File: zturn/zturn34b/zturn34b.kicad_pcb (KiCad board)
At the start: 4 copper layers, 56.5 x 54 mm, 27 parts, among them U1 74AXP4T245, U2 74AXP4T245, U3 74AXP4T245, U4 74AXP4T245, U5 74AXP4T245

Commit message: update net names on zturn pcbs to match active high/low signal type
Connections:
- net /_rMA renamed /r_MA
- net /iBEMA renamed /i_BEMA
- net /iMEM07 renamed /iMEM_07
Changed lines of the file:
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@@
   (net 13 "/pMA07")
   (net 14 "/i_MEMDONE")
-  (net 15 "/_rMA")
+  (net 15 "/r_MA")
   (net 16 "unconnected-(U5-2B1-Pad11)")
   (net 17 "unconnected-(U5-1B1-Pad13)")
@@
   (net 33 "/MEMBUSN")
   (net 34 "/x_MEM")
-  (net 35 "/iBEMA")
-  (net 36 "/iMEM07")
+  (net 35 "/i_BEMA")
+  (net 36 "/iMEM_07")
   (net 37 "/i_EMA")
   (net 38 "/j_STROBE")
@@
       (net 34 "/x_MEM") (pinfunction "Pin_21") (pintype "passive"))
     (pad "22" thru_hole oval (at 2.54 25.4 90) (size 1.7 1.7) (drill 1) (layers "*.Cu" "*.Mask")
-      (net 15 "/_rMA") (pinfunction "Pin_22") (pintype "passive"))
+      (net 15 "/r_MA") (pinfunction "Pin_22") (pintype "passive"))
     (pad "23" thru_hole oval (at 0 27.94 90) (size 1.7 1.7) (drill 1) (layers "*.Cu" "*.Mask")
       (net 19 "GND") (pinfunction "Pin_23") (pintype "passive"))
@@
       (net 19 "GND") (pinfunction "Pin_24") (pintype "passive"))
     (pad "25" thru_hole oval (at 0 30.48 90) (size 1.7 1.7) (drill 1) (layers "*.Cu" "*.Mask")
-      (net 35 "/iBEMA") (pinfunction "Pin_25") (pintype "passive"))
+      (net 35 "/i_BEMA") (pinfunction "Pin_25") (pintype "passive"))
     (pad "26" thru_hole oval (at 2.54 30.48 90) (size 1.7 1.7) (drill 1) (layers "*.Cu" "*.Mask")
-      (net 36 "/iMEM07") (pinfunction "Pin_26") (pintype "passive"))
+      (net 36 "/iMEM_07") (pinfunction "Pin_26") (pintype "passive"))
     (pad "27" thru_hole oval (at 0 33.02 90) (size 1.7 1.7) (drill 1) (layers "*.Cu" "*.Mask")
       (net 19 "GND") (pinfunction "Pin_27") (pintype "passive"))
@@
       (net 10 "/pMA04") (pinfunction "1B1") (pintype "tri_state"))
     (pad "14" smd roundrect (at 2.8625 -0.975 90) (size 1.475 0.4) (layers "F.Cu" "F.Paste" "F.Mask") (roundrect_rratio 0.25)
-      (net 15 "/_rMA") (pinfunction "2OE") (pintype "input"))
+      (net 15 "/r_MA") (pinfunction "2OE") (pintype "input"))
     (pad "15" smd roundrect (at 2.8625 -1.625 90) (size 1.475 0.4) (layers "F.Cu" "F.Paste" "F.Mask") (roundrect_rratio 0.25)
-      (net 15 "/_rMA") (pinfunction "1OE") (pintype "input"))
+      (net 15 "/r_MA") (pinfunction "1OE") (pintype "input"))
     (pad "16" smd roundrect (at 2.8625 -2.275 90) (size 1.475 0.4) (layers "F.Cu" "F.Paste" "F.Mask") (roundrect_rratio 0.25)
       (net 20 "+5V") (pinfunction "VCCB") (pintype "power_in"))
@@
       (net 2 "/pMA00") (pinfunction "1B1") (pintype "tri_state"))
     (pad "14" smd roundrect (at 2.8625 -0.975 90) (size 1.475 0.4) (layers "F.Cu" "F.Paste" "F.Mask") (roundrect_rratio 0.25)
-      (net 15 "/_rMA") (pinfunction "2OE") (pintype "input"))
+      (net 15 "/r_MA") (pinfunction "2OE") (pintype "input"))
     (pad "15" smd roundrect (at 2.8625 -1.625 90) (size 1.475 0.4) (layers "F.Cu" "F.Paste" "F.Mask") (roundrect_rratio 0.25)
-      (net 15 "/_rMA") (pinfunction "1OE") (pintype "input"))
+      (net 15 "/r_MA") (pinfunction "1OE") (pintype "input"))
     (pad "16" smd roundrect (at 2.8625 -2.275 90) (size 1.475 0.4) (layers "F.Cu" "F.Paste" "F.Mask") (roundrect_rratio 0.25)
       (net 20 "+5V") (pinfunction "VCCB") (pintype "power_in"))
@@
       (net 47 "+3V3") (pintype "passive"))
     (pad "2" smd roundrect (at 0.32 0 180) (size 0.46 0.4) (layers "B.Cu" "B.Mask") (roundrect_rratio 0.25)
-      (net 15 "/_rMA") (pintype "passive"))
+      (net 15 "/r_MA") (pintype "passive"))
     (model "${KICAD6_3DMODEL_DIR}/Resistor_SMD.3dshapes/R_0201_0603Metric.wrl"
       (offset (xyz 0 0 0))
@@
       (net 9 "/pMA11") (pinfunction "1B1") (pintype "tri_state"))
     (pad "14" smd roundrect (at 2.8625 0.975 90) (size 1.475 0.4) (layers "B.Cu" "B.Paste" "B.Mask") (roundrect_rratio 0.25)
-      (net 15 "/_rMA") (pinfunction "2OE") (pintype "input"))
+      (net 15 "/r_MA") (pinfunction "2OE") (pintype "input"))
     (pad "15" smd roundrect (at 2.8625 1.625 90) (size 1.475 0.4) (layers "B.Cu" "B.Paste" "B.Mask") (roundrect_rratio 0.25)
-      (net 15 "/_rMA") (pinfunction "1OE") (pintype "input"))
+      (net 15 "/r_MA") (pinfunction "1OE") (pintype "input"))
     (pad "16" smd roundrect (at 2.8625 2.275 90) (size 1.475 0.4) (layers "B.Cu" "B.Paste" "B.Mask") (roundrect_rratio 0.25)
       (net 20 "+5V") (pinfunction "VCCB") (pintype "power_in"))

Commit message: update software and further updates to firmware/pcbs
...for invertering transistors

./z8lsimtest works
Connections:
- net /iMEM_07 renamed /i_MEM_07
- net /i_BEMA renamed /iBEMA
- net /i_EMA renamed /iEMA
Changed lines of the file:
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@@
   (net 33 "/MEMBUSN")
   (net 34 "/x_MEM")
-  (net 35 "/i_BEMA")
-  (net 36 "/iMEM_07")
-  (net 37 "/i_EMA")
+  (net 35 "/iBEMA")
+  (net 36 "/i_MEM_07")
+  (net 37 "/iEMA")
   (net 38 "/j_STROBE")
   (net 39 "/j_EA")
@@
       (net 19 "GND") (pinfunction "Pin_24") (pintype "passive"))
     (pad "25" thru_hole oval (at 0 30.48 90) (size 1.7 1.7) (drill 1) (layers "*.Cu" "*.Mask")
-      (net 35 "/i_BEMA") (pinfunction "Pin_25") (pintype "passive"))
+      (net 35 "/iBEMA") (pinfunction "Pin_25") (pintype "passive"))
     (pad "26" thru_hole oval (at 2.54 30.48 90) (size 1.7 1.7) (drill 1) (layers "*.Cu" "*.Mask")
-      (net 36 "/iMEM_07") (pinfunction "Pin_26") (pintype "passive"))
+      (net 36 "/i_MEM_07") (pinfunction "Pin_26") (pintype "passive"))
     (pad "27" thru_hole oval (at 0 33.02 90) (size 1.7 1.7) (drill 1) (layers "*.Cu" "*.Mask")
       (net 19 "GND") (pinfunction "Pin_27") (pintype "passive"))
@@
       (net 19 "GND") (pinfunction "Pin_28") (pintype "passive"))
     (pad "29" thru_hole oval (at 0 35.56 90) (size 1.7 1.7) (drill 1) (layers "*.Cu" "*.Mask")
-      (net 37 "/i_EMA") (pinfunction "Pin_29") (pintype "passive"))
+      (net 37 "/iEMA") (pinfunction "Pin_29") (pintype "passive"))
     (pad "30" thru_hole oval (at 2.54 35.56 90) (size 1.7 1.7) (drill 1) (layers "*.Cu" "*.Mask")
       (net 1 "/i_EA") (pinfunction "Pin_30") (pintype "passive"))

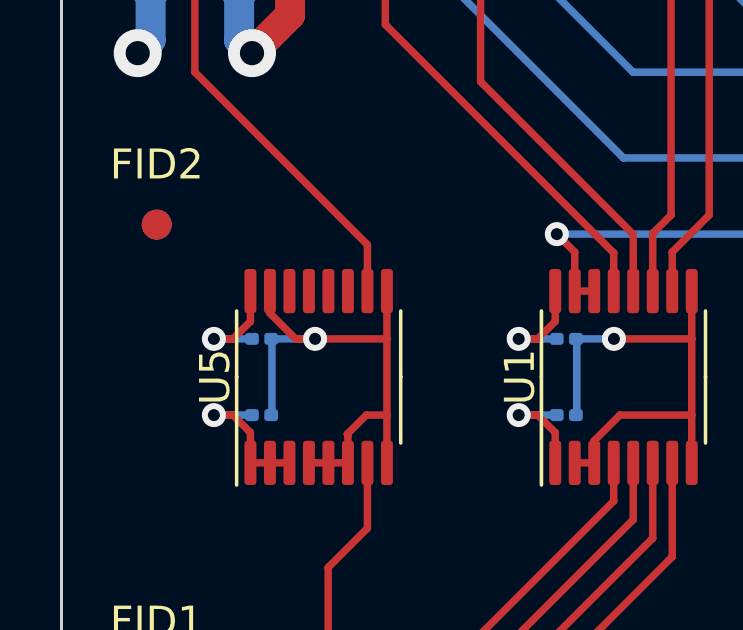
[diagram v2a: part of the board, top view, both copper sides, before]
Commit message: fixed polarity of bus signals for the open-drain transistors
    PDP         Zynq
    MEM         _MEM
    MEM_P       _MEM_P
    _DMAADDR    DMAADDR
    _DMADATA    DMADATA
    _INPUTBUS   INPUTBUS

Also fixed MEMINCR polarity and fixed missing ground connection on circuit board.
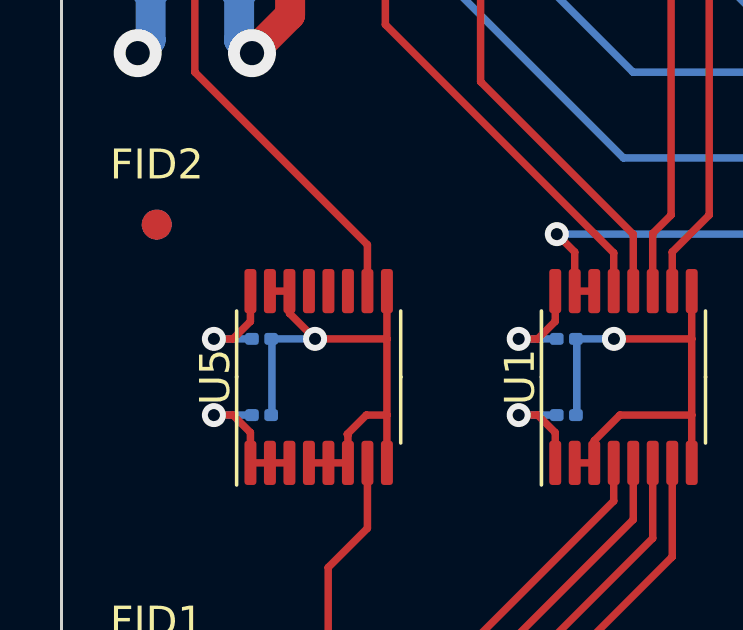
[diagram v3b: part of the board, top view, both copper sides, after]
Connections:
- U5 pad 14: unconnected-(U5-2OE-Pad14) -> GND

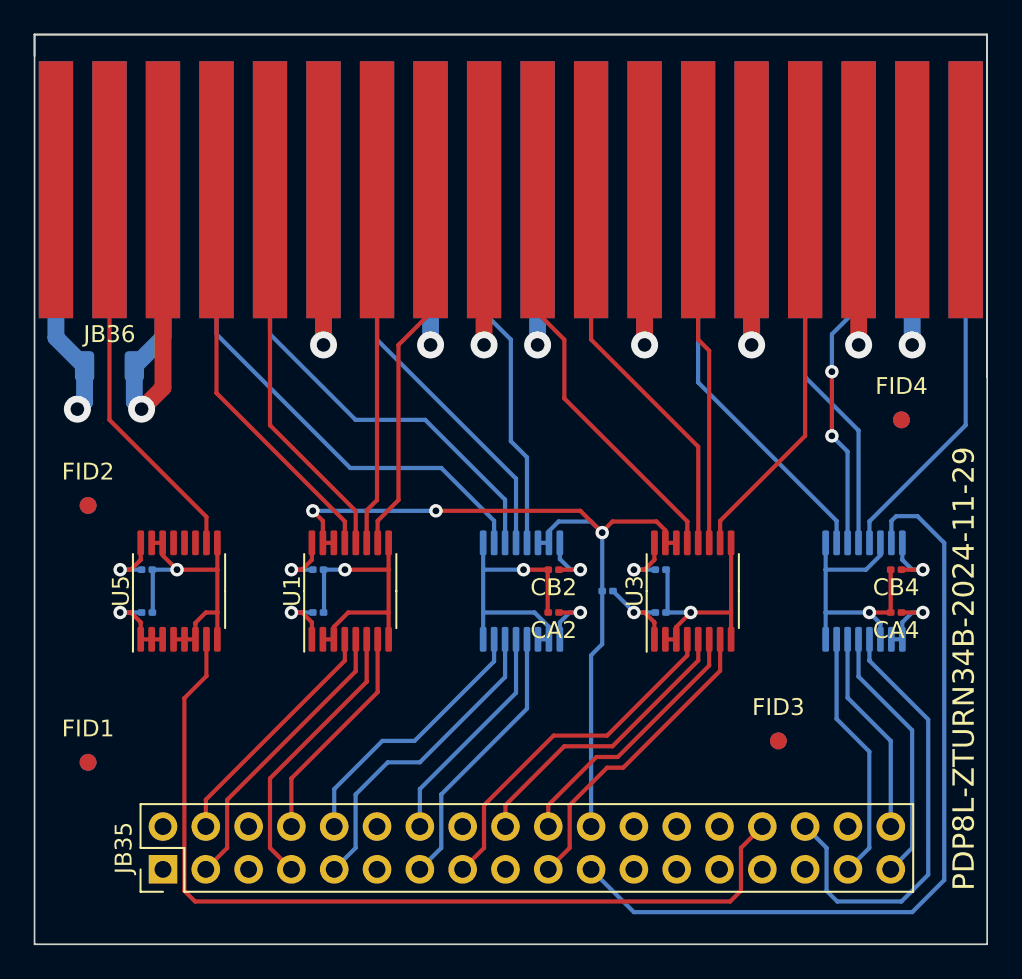
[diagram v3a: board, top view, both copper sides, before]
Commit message: update zturn34b pcb legend and clean up some traces
fixed the i_EA driver output enable dec 26, but legend not updated
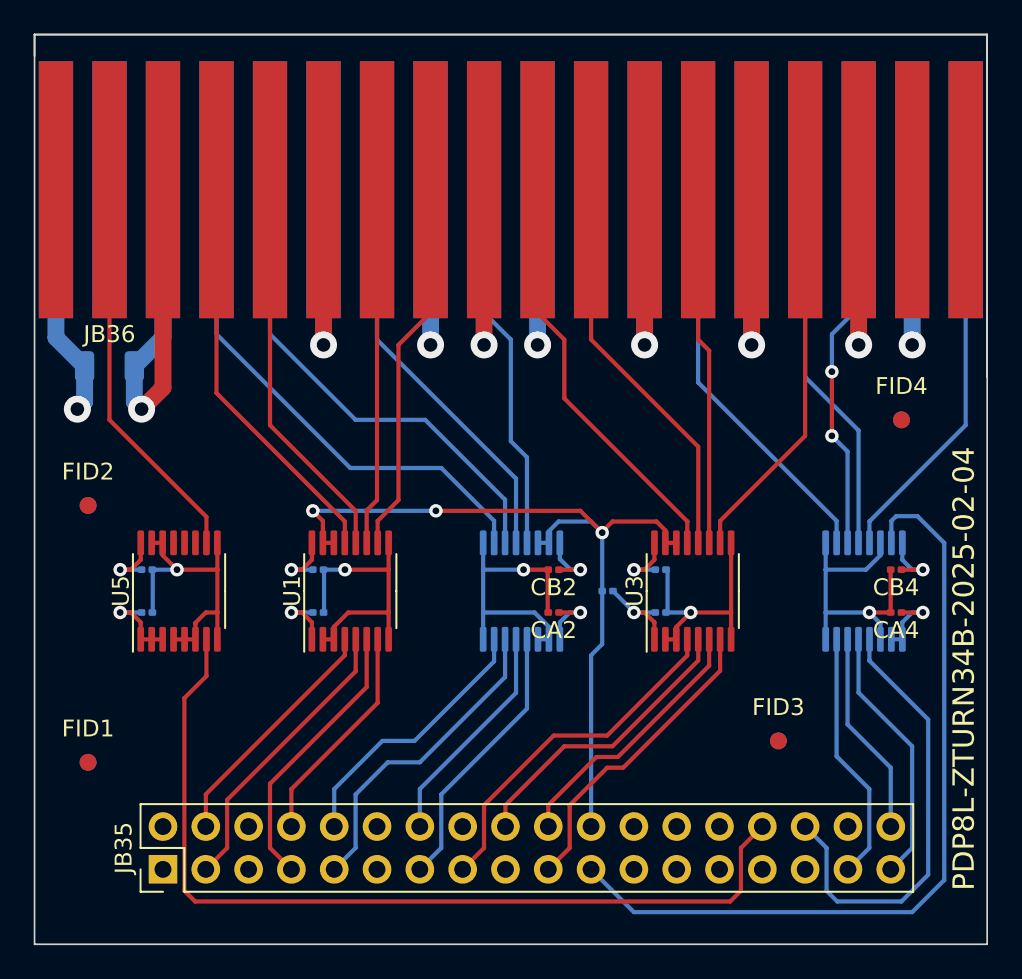
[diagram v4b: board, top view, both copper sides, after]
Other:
- board text added: "PDP8L-ZTURN34B-2025-02-04"
- board text removed: "PDP8L-ZTURN34B-2024-11-29"
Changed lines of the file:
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@@
   (gr_line (start 56.515 53.975) (end 0 53.975)
     (stroke (width 0.1) (type default)) (layer "Edge.Cuts"))
-  (gr_text "PDP8L-ZTURN34B-2024-11-29" (at 55.88 50.8 90) (layer "F.SilkS")
+  (gr_text "PDP8L-ZTURN34B-2025-02-04" (at 55.88 50.8 90) (layer "F.SilkS")
     (effects (font (size 1.27 1.27) (thickness 0.15)) (justify left bottom))
   )
@@
   (segment (start 19.0575 37.775) (end 11.43 45.4025) (width 0.25) (layer "F.Cu") (net 20))
   (segment (start 11.43 45.4025) (end 11.43 48.26) (width 0.25) (layer "F.Cu") (net 20))
-  (segment (start 18.4075 35.8825) (end 18.4075 37.155) (width 0.25) (layer "F.Cu") (net 21))
-  (segment (start 18.4075 37.155) (end 10.16 45.4025) (width 0.25) (layer "F.Cu") (net 21))
-  (segment (start 10.16 45.4025) (end 10.16 46.99) (width 0.25) (layer "F.Cu") (net 21))
-  (segment (start 13.97 44.1325) (end 13.97 48.26) (width 0.25) (layer "F.Cu") (net 22))
-  (segment (start 19.7075 38.395) (end 13.97 44.1325) (width 0.25) (layer "F.Cu") (net 22))
-  (segment (start 19.7075 35.8825) (end 19.7075 38.395) (width 0.25) (layer "F.Cu") (net 22))
-  (segment (start 13.97 48.26) (end 15.24 49.53) (width 0.25) (layer "F.Cu") (net 22))
-  (segment (start 20.3575 35.8825) (end 20.3575 39.015) (width 0.25) (layer "F.Cu") (net 23))
-  (segment (start 15.24 44.1325) (end 15.24 46.99) (width 0.25) (layer "F.Cu") (net 23))
-  (segment (start 20.3575 39.015) (end 15.24 44.1325) (width 0.25) (layer "F.Cu") (net 23))
+  (segment (start 10.16 45.0775) (end 10.16 46.99) (width 0.25) (layer "F.Cu") (net 21))
+  (segment (start 18.4075 35.8825) (end 18.4075 36.83) (width 0.25) (layer "F.Cu") (net 21))
+  (segment (start 18.4075 36.83) (end 10.16 45.0775) (width 0.25) (layer "F.Cu") (net 21))
+  (segment (start 13.97 48.26) (end 13.97 44.45) (width 0.25) (layer "F.Cu") (net 22))
+  (segment (start 13.97 44.45) (end 19.7075 38.7125) (width 0.25) (layer "F.Cu") (net 22))
+  (segment (start 19.7075 38.7125) (end 19.7075 35.8825) (width 0.25) (layer "F.Cu") (net 22))
+  (segment (start 15.24 49.53) (end 13.97 48.26) (width 0.25) (layer "F.Cu") (net 22))
+  (segment (start 20.3575 39.65) (end 20.3575 35.8825) (width 0.25) (layer "F.Cu") (net 23))
+  (segment (start 15.24 46.99) (end 15.24 44.7675) (width 0.25) (layer "F.Cu") (net 23))
+  (segment (start 15.24 44.7675) (end 20.3575 39.65) (width 0.25) (layer "F.Cu") (net 23))
   (segment (start 19.05 48.26) (end 19.05 45.085) (width 0.25) (layer "B.Cu") (net 24))
   (segment (start 20.955 43.18) (end 22.86 43.18) (width 0.25) (layer "B.Cu") (net 24))
@@
   (segment (start 20.6375 41.91) (end 22.5425 41.91) (width 0.25) (layer "B.Cu") (net 25))
   (segment (start 17.78 44.7675) (end 20.6375 41.91) (width 0.25) (layer "B.Cu") (net 25))
-  (segment (start 52.07 41.275) (end 48.8875 38.0925) (width 0.25) (layer "B.Cu") (net 26))
-  (segment (start 48.8875 38.0925) (end 48.8875 35.8825) (width 0.25) (layer "B.Cu") (net 26))
-  (segment (start 52.07 48.26) (end 52.07 41.275) (width 0.25) (layer "B.Cu") (net 26))
+  (segment (start 52.07 42.2275) (end 48.8875 39.045) (width 0.25) (layer "B.Cu") (net 26))
   (segment (start 50.8 49.53) (end 52.07 48.26) (width 0.25) (layer "B.Cu") (net 26))
+  (segment (start 48.8875 39.045) (end 48.8875 35.8825) (width 0.25) (layer "B.Cu") (net 26))
+  (segment (start 52.07 48.26) (end 52.07 42.2275) (width 0.25) (layer "B.Cu") (net 26))
   (segment (start 29.2175 39.9975) (end 29.2175 35.8825) (width 0.25) (layer "B.Cu") (net 27))
   (segment (start 24.13 48.26) (end 24.13 45.085) (width 0.25) (layer "B.Cu") (net 27))
@@
   (segment (start 47.3075 17.78) (end 48.895 16.1925) (width 0.25) (layer "B.Cu") (net 42))
   (segment (start 47.3075 23.8125) (end 48.2375 24.7425) (width 0.25) (layer "B.Cu") (net 42))
-  (segment (start 49.53 42.545) (end 49.53 48.26) (width 0.25) (layer "B.Cu") (net 45))
-  (segment (start 49.53 48.26) (end 48.26 49.53) (width 0.25) (layer "B.Cu") (net 45))
-  (segment (start 47.5875 40.6025) (end 49.53 42.545) (width 0.25) (layer "B.Cu") (net 45))
-  (segment (start 47.5875 35.8825) (end 47.5875 40.6025) (width 0.25) (layer "B.Cu") (net 45))
+  (segment (start 48.26 49.53) (end 49.53 48.26) (width 0.25) (layer "B.Cu") (net 45))
+  (segment (start 49.53 44.7675) (end 47.5875 42.825) (width 0.25) (layer "B.Cu") (net 45))
+  (segment (start 49.53 48.26) (end 49.53 44.7675) (width 0.25) (layer "B.Cu") (net 45))
+  (segment (start 47.5875 42.825) (end 47.5875 35.8825) (width 0.25) (layer "B.Cu") (net 45))
   (segment (start 5.715 34.29) (end 6.2975 34.8725) (width 0.25) (layer "F.Cu") (net 46))
   (segment (start 6.2975 35.8825) (end 6.9475 35.8825) (width 0.25) (layer "F.Cu") (net 46))
@@
   (segment (start 49.5375 30.1575) (end 49.5375 28.885) (width 0.25) (layer "B.Cu") (net 47))
   (segment (start 55.245 23.1775) (end 55.245 9.2075) (width 0.25) (layer "B.Cu") (net 47))
-  (segment (start 48.2375 39.3475) (end 50.8 41.91) (width 0.25) (layer "B.Cu") (net 48))
-  (segment (start 50.8 41.91) (end 50.8 46.99) (width 0.25) (layer "B.Cu") (net 48))
-  (segment (start 48.2375 35.8825) (end 48.2375 39.3475) (width 0.25) (layer "B.Cu") (net 48))
+  (segment (start 48.2375 40.935) (end 48.2375 35.8825) (width 0.25) (layer "B.Cu") (net 48))
+  (segment (start 50.8 46.99) (end 50.8 43.4975) (width 0.25) (layer "B.Cu") (net 48))
+  (segment (start 50.8 43.4975) (end 48.2375 40.935) (width 0.25) (layer "B.Cu") (net 48))
   (zone (net 46) (net_name "+3V3") (layer "In1.Cu") (hatch edge 0.5)
     (priority 2)
@@
       (pts
         (xy 0.635 33.655)
-        (xy 189.23 33.655)
-        (xy 189.23 53.34)
+        (xy 55.88 33.655)
+        (xy 55.88 53.34)
         (xy 0.635 53.34)
       )
@@
       (pts
         (xy 0.635 17.145)
-        (xy 189.23 17.145)
-        (xy 189.23 32.385)
+        (xy 55.88 17.145)
+        (xy 55.88 32.385)
         (xy 0.635 32.385)
       )
@@
       (pts
         (xy 0.635 17.145)
-        (xy 189.23 17.145)
-        (xy 189.23 53.34)
+        (xy 55.88 17.145)
+        (xy 55.88 53.34)
         (xy 0.635 53.34)
       )
